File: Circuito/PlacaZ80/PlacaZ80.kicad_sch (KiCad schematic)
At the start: 28 parts, among them J1 Conn_01x04_Pin, J2 Conn_01x14_Socket, U1 74HC00, U2 74HC138, U3 74LS08, U4 DS1233-05, U5 74HC02, U6 Z80CPU, U7 28C16, U8 6116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

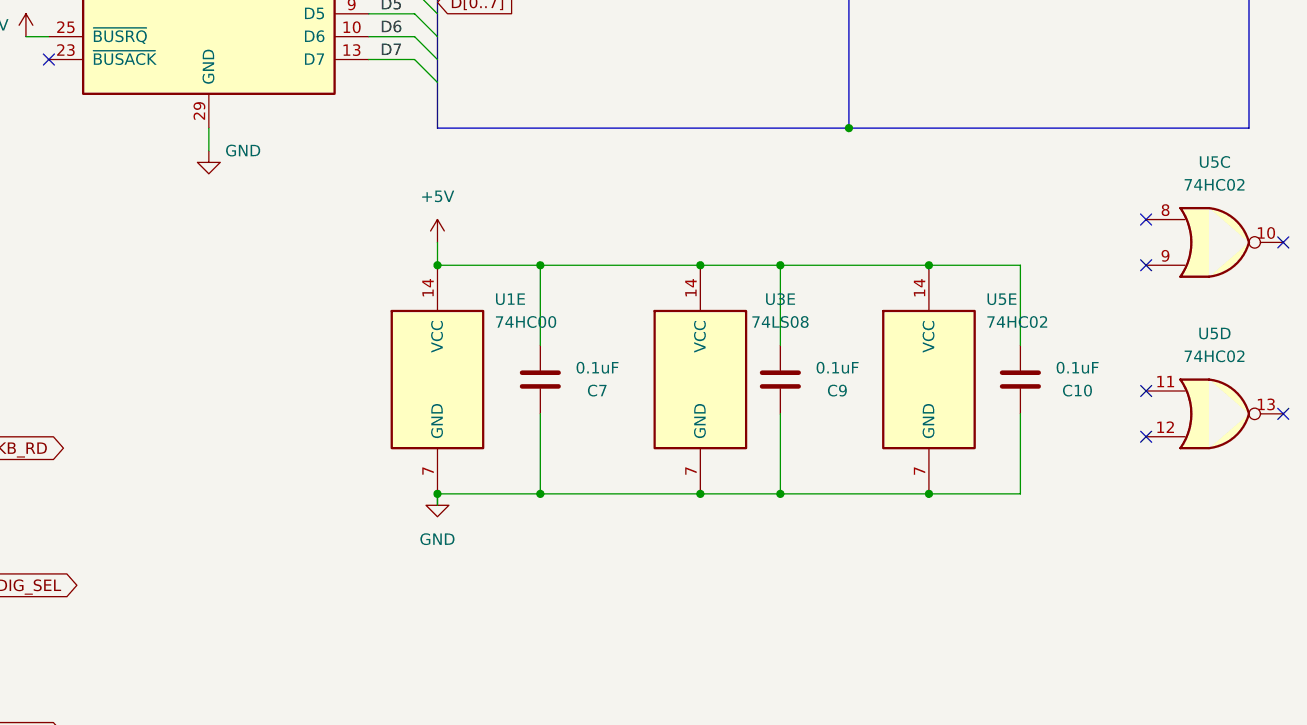
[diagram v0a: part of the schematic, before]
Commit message: Acréscimo da Placa de IO e o teste do Display
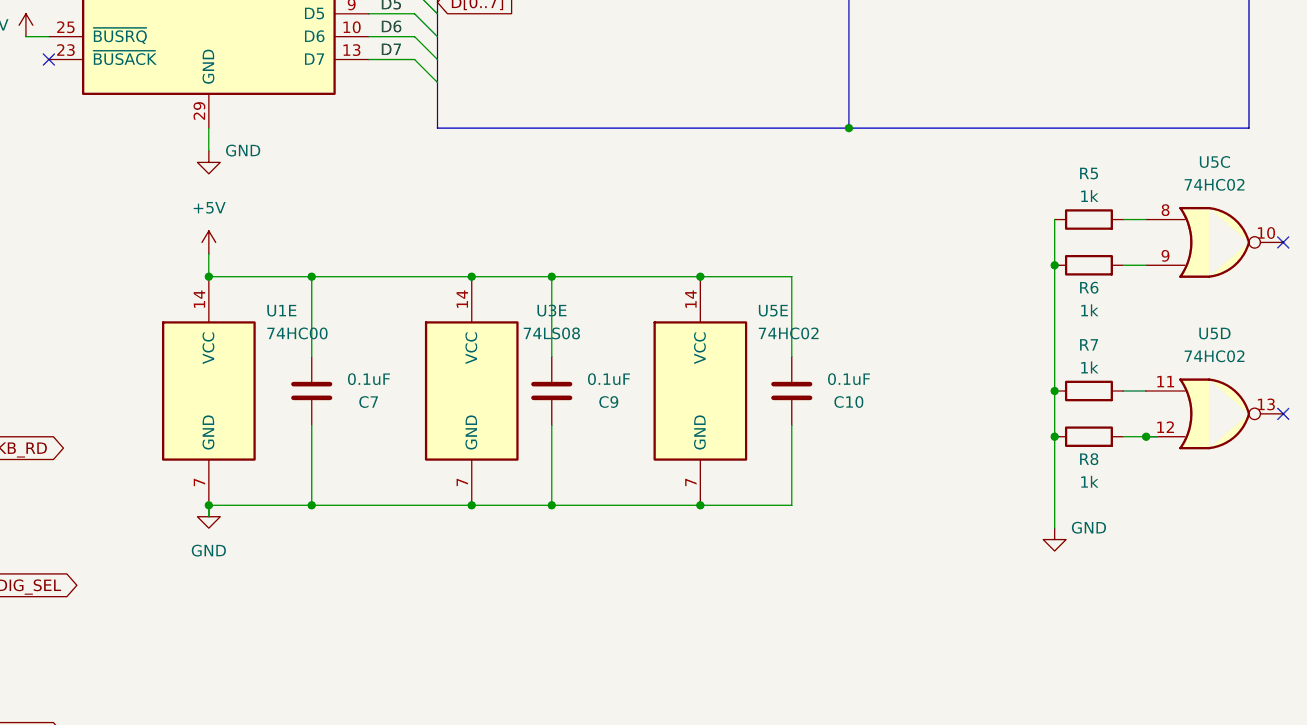
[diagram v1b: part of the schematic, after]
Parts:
- added R5, R6, R7, R8: 1k, Resistor_THT:R_Axial_DIN0207_L6.3mm_D2.5mm_P10.16mm_Horizontal, symbol Device:R
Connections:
- net GND: now also R5.1, R6.1, R7.1, R8.1
- net at U5.11: now also R7.2
- net at U5.12: now also R8.2
- net at U5.8: now also R5.2
- net at U5.9: now also R6.2
- no-connect marks 18 -> 14
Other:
- moved on the sheet: C10, C7, C9, U1E, U3E, U5E
